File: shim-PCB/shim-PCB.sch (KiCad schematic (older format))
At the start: 24 parts, among them J1 ROMI-Encoder, J10 LineSensor, J11 LineSensor, J12 SPI, J13 Ultrasonic., J14 THING, J15 THING, J16 Conn_01x02_Female, J2 ROMI-Encoder, J3 Conn_01x19_Female, J4 ServoAnalog, J5 Conn_01x19_Female, J6 Conn_01x19_Female, J7 ROMI, J8 ROMI, J9 Conn_01x19_Female

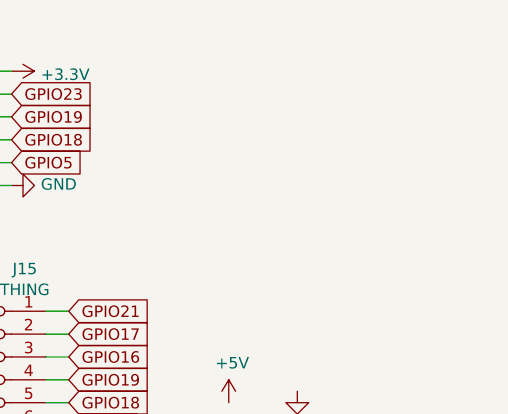
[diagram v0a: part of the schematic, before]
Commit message: Broke out i2c
ISsue #7
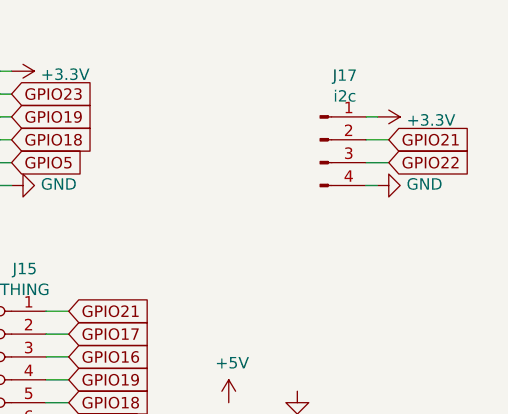
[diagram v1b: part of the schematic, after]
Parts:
- added J17: i2c, Connector_PinSocket_2.54mm:PinSocket_1x04_P2.54mm_Vertical, symbol Connector:Conn_01x04_Male
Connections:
- net +3V3: now also J17.1 (Pin_1)
- net GND: now also J17.4 (Pin_4)
- net GPIO21: now also J17.2 (Pin_2)
- net GPIO22: now also J17.3 (Pin_3)
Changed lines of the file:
@@
 Text Notes 1000 6550 1    50   ~ 0
 Right
+$Comp
+L Connector:Conn_01x04_Male J17
+U 1 1 5F351CBA
+P 7700 1200
+F 0 "J17" H 7808 1481 50  0000 C CNN
+F 1 "i2c" H 7808 1390 50  0000 C CNN
+F 2 "Connector_PinSocket_2.54mm:PinSocket_1x04_P2.54mm_Vertical" H 7700 1200 50  0001 C CNN
+F 3 "~" H 7700 1200 50  0001 C CNN
+	1    7700 1200
+	1    0    0    -1
+$EndComp
+$Comp
+L power:+3.3V #PWR0137
+U 1 1 5F351CC0
+P 7950 1100
+F 0 "#PWR0137" H 7950 950 50  0001 C CNN
+F 1 "+3.3V" V 7965 1228 50  0000 L CNN
+F 2 "" H 7950 1100 50  0001 C CNN
+F 3 "" H 7950 1100 50  0001 C CNN
+	1    7950 1100
+	0    1    1    0
+$EndComp
+$Comp
+L power:GND #PWR0138
+U 1 1 5F351CC6
+P 7950 1400
+F 0 "#PWR0138" H 7950 1150 50  0001 C CNN
+F 1 "GND" V 7955 1272 50  0000 R CNN
+F 2 "" H 7950 1400 50  0001 C CNN
+F 3 "" H 7950 1400 50  0001 C CNN
+	1    7950 1400
+	0    -1   -1   0
+$EndComp
+Wire Wire Line
+	7950 1100 7900 1100
+Wire Wire Line
+	7950 1400 7900 1400
+Text GLabel 8000 1200 2    50   Input ~ 0
+GPIO21
+Text GLabel 8000 1300 2    50   Input ~ 0
+GPIO22
+Wire Wire Line
+	8000 1200 7900 1200
+Wire Wire Line
+	8000 1300 7900 1300
 $EndSCHEMATC

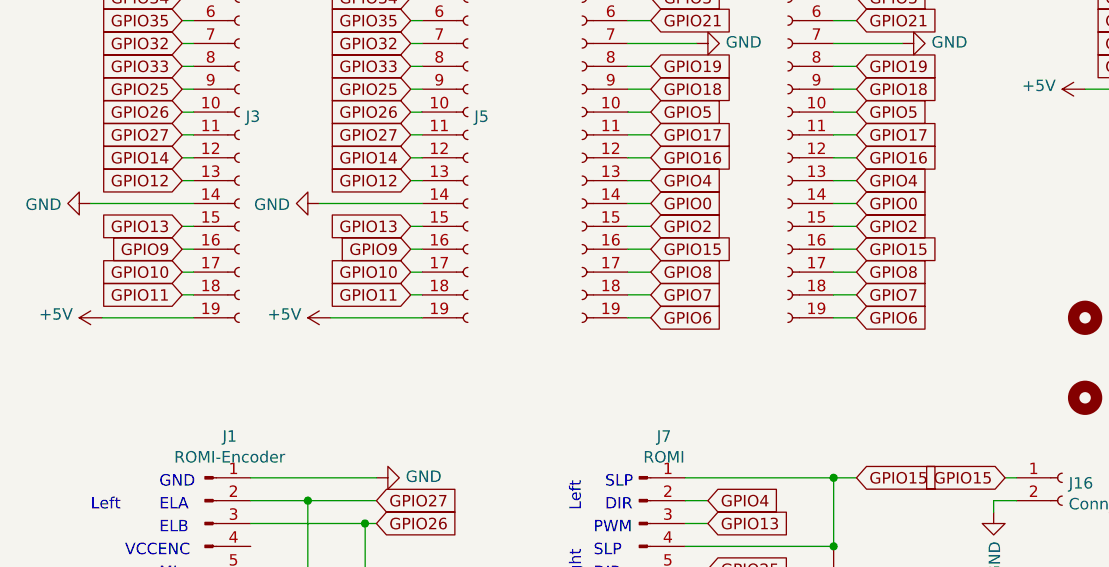
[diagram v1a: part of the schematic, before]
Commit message: Switched to 4 layer. Disconnected flash pins.
Resolved #15
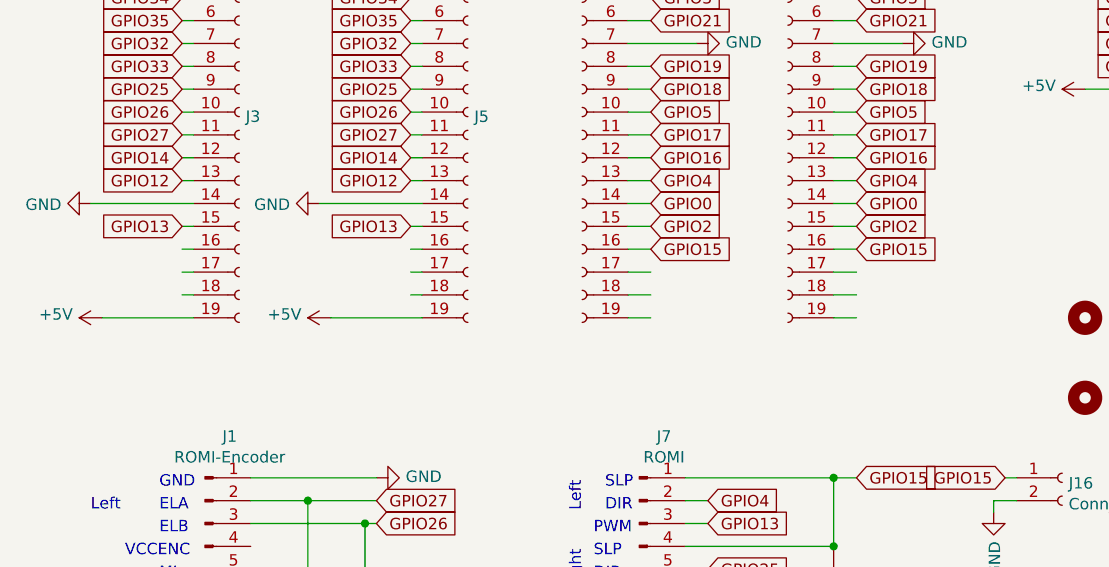
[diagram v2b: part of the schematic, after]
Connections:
- net labels removed: GPIO10, GPIO11, GPIO6, GPIO7, GPIO8, GPIO9
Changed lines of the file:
@@
 Text GLabel 2250 3450 0    50   Input ~ 0
 GPIO13
-Text GLabel 2250 3550 0    50   Input ~ 0
-GPIO9
-Text GLabel 2250 3650 0    50   Input ~ 0
-GPIO10
-Text GLabel 2250 3750 0    50   Input ~ 0
-GPIO11
 $Comp
 L power:+5V #PWR0108
@@
 Text GLabel 3300 3550 2    50   Input ~ 0
 GPIO15
-Text GLabel 3300 3650 2    50   Input ~ 0
-GPIO8
-Text GLabel 3300 3750 2    50   Input ~ 0
-GPIO7
-Text GLabel 3300 3850 2    50   Input ~ 0
-GPIO6
 $Comp
 L power:GND #PWR0129
@@
 Text GLabel 1250 3450 0    50   Input ~ 0
 GPIO13
-Text GLabel 1250 3550 0    50   Input ~ 0
-GPIO9
-Text GLabel 1250 3650 0    50   Input ~ 0
-GPIO10
-Text GLabel 1250 3750 0    50   Input ~ 0
-GPIO11
 $Comp
 L power:+5V #PWR0132
@@
 Text GLabel 4200 3550 2    50   Input ~ 0
 GPIO15
-Text GLabel 4200 3650 2    50   Input ~ 0
-GPIO8
-Text GLabel 4200 3750 2    50   Input ~ 0
-GPIO7
-Text GLabel 4200 3850 2    50   Input ~ 0
-GPIO6
 $Comp
 L power:GND #PWR0134

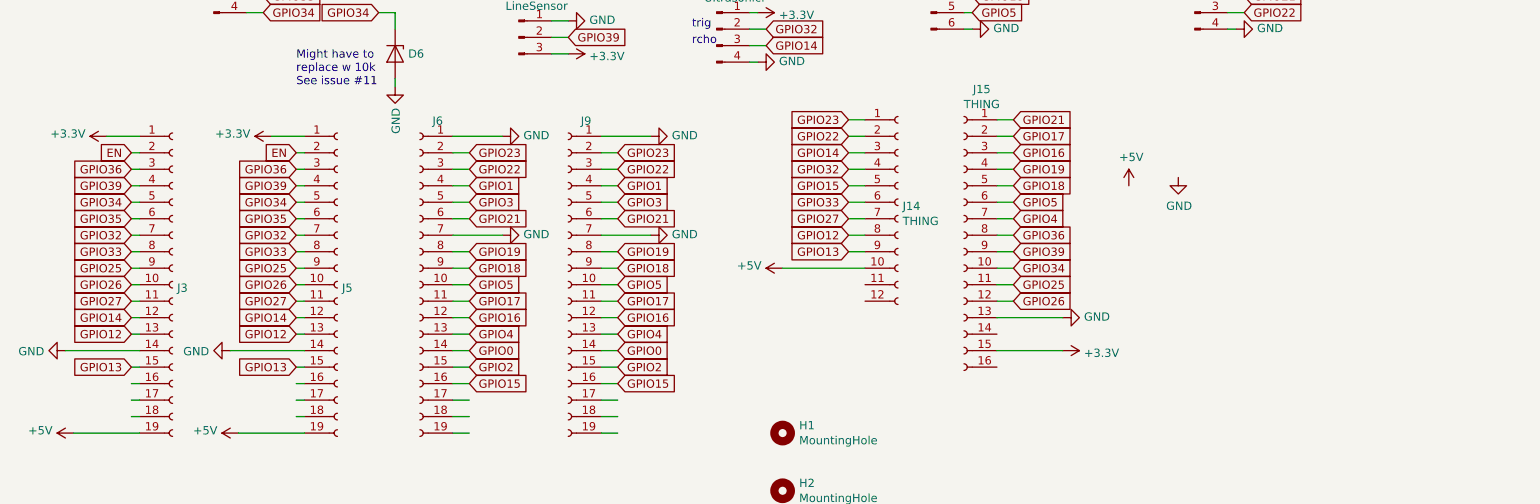
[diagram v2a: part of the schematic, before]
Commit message: Fixed silkscreen
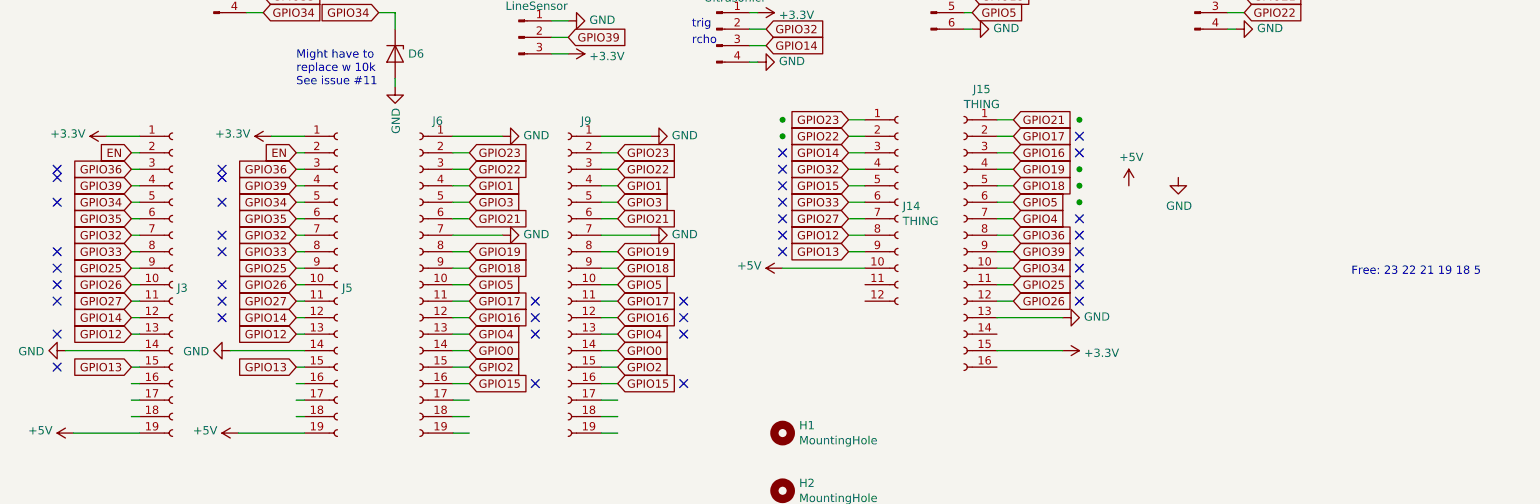
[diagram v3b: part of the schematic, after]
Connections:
- no-connect marks 0 -> 40
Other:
- note added: "Free: 23 22 21 19 18 5"
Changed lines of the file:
@@
 Wire Wire Line
 	8000 1300 7900 1300
+NoConn ~ 1800 2750
+NoConn ~ 1800 2450
+NoConn ~ 800  2450
+NoConn ~ 800  2750
+NoConn ~ 5200 2450
+NoConn ~ 7000 2850
+NoConn ~ 800  2250
+NoConn ~ 800  2300
+NoConn ~ 1800 2250
+NoConn ~ 1800 2300
+NoConn ~ 7000 2650
+NoConn ~ 7000 2750
+NoConn ~ 5200 2150
+NoConn ~ 5200 2250
+NoConn ~ 1800 2650
+NoConn ~ 1800 3150
+NoConn ~ 800  3050
+NoConn ~ 800  2950
+NoConn ~ 3700 3050
+NoConn ~ 3700 3150
+NoConn ~ 4600 3050
+NoConn ~ 4600 3150
+NoConn ~ 7000 2050
+NoConn ~ 7000 2150
+NoConn ~ 1800 3050
+NoConn ~ 1800 2950
+NoConn ~ 5200 2550
+NoConn ~ 7000 3050
+NoConn ~ 7000 2550
+NoConn ~ 5200 2750
+NoConn ~ 4600 3250
+NoConn ~ 800  3450
+NoConn ~ 3700 3250
+NoConn ~ 7000 2950
+NoConn ~ 5200 2650
+NoConn ~ 800  2850
+NoConn ~ 800  3250
+NoConn ~ 3700 3550
+NoConn ~ 4600 3550
+NoConn ~ 5200 2350
+Text Notes 8650 2900 0    50   ~ 0
+Free: 23 22 21 19 18 5
+Connection ~ 5200 1950
+Connection ~ 5200 2050
+Connection ~ 7000 1950
+Connection ~ 7000 2250
+Connection ~ 7000 2350
+Connection ~ 7000 2450
 $EndSCHEMATC

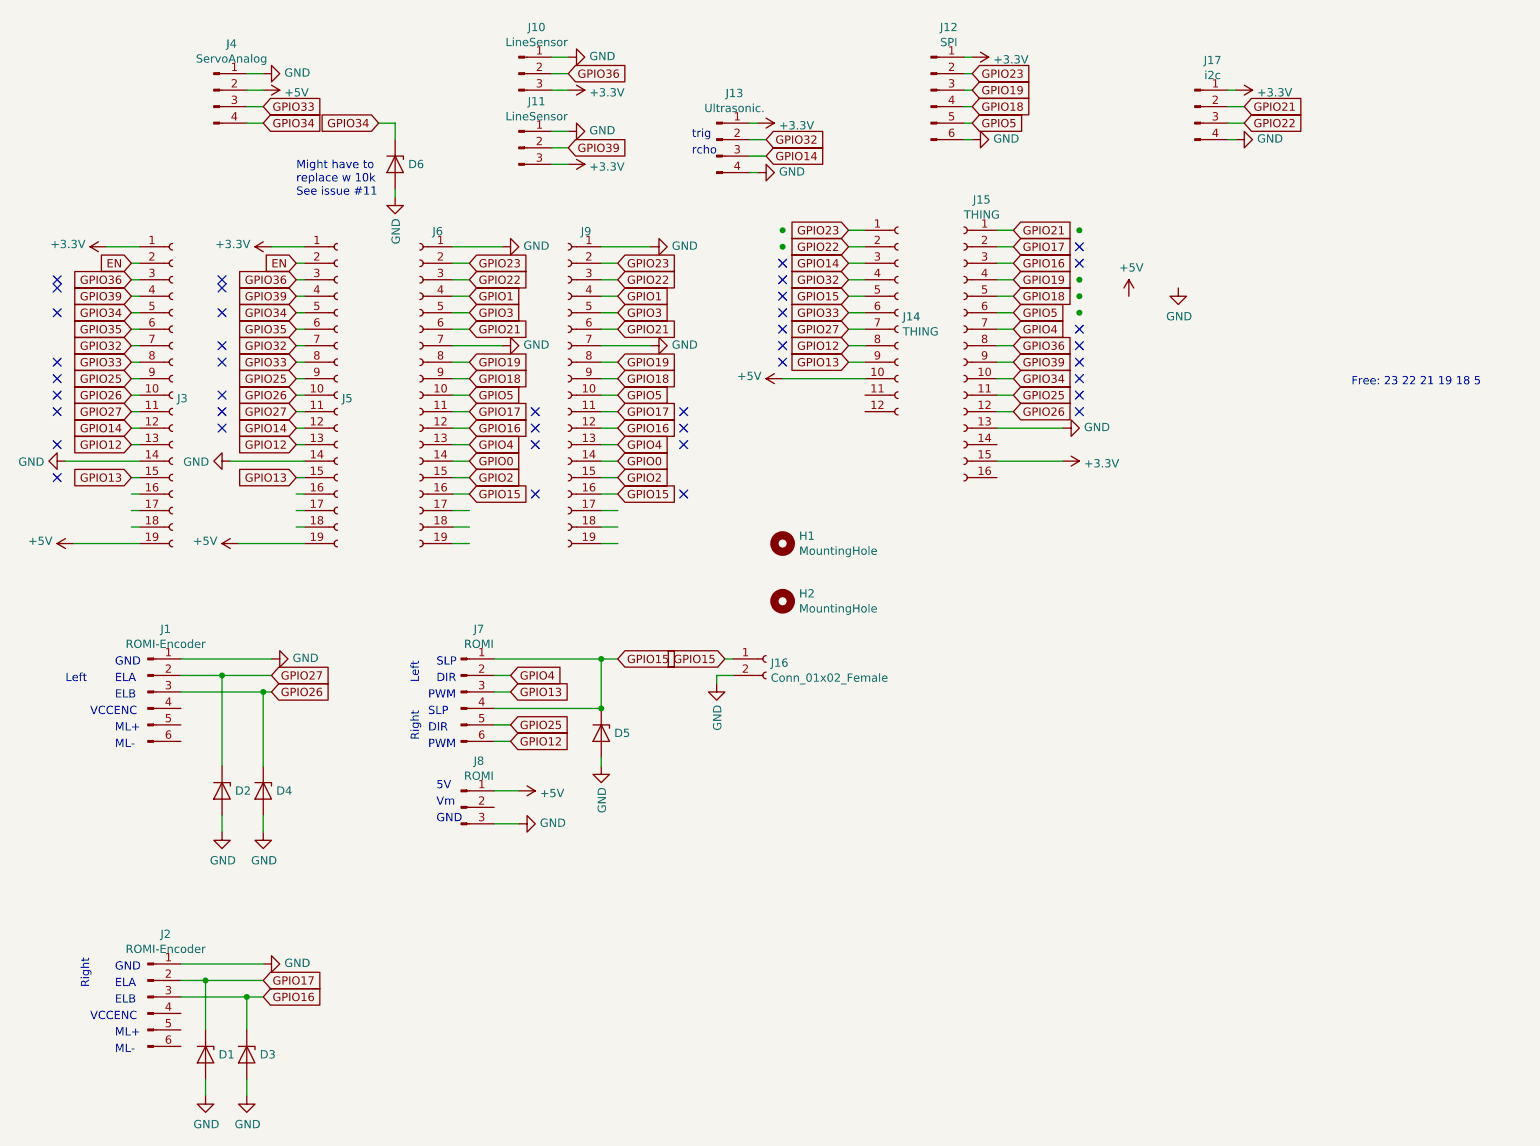
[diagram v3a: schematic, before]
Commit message: new board rev
Added jumper to switch between pins 21 and 23 to resolve conflict with samd21 i2c resolving issue #26

Swapped encoder and ultrasonic pins to resolve conflict with samd21 resolving issue #25
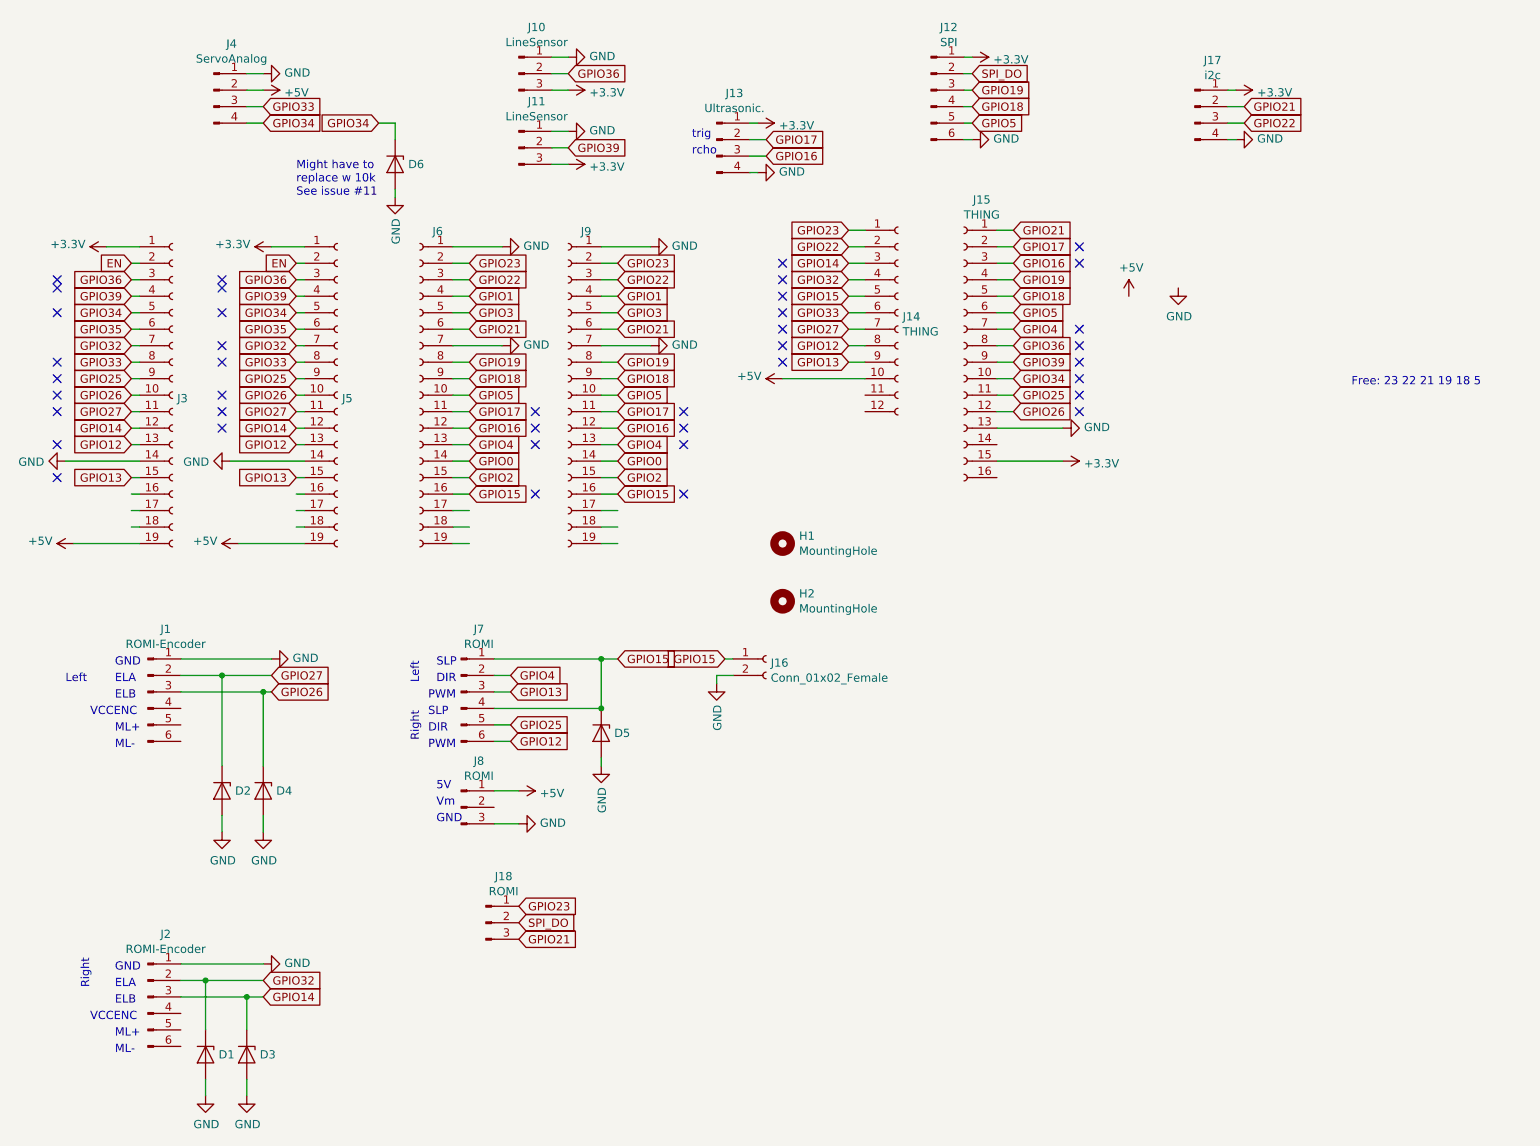
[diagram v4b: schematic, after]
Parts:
- added J18: ROMI, Connector_PinSocket_2.54mm:PinSocket_1x03_P2.54mm_Vertical, symbol Connector:Conn_01x03_Male
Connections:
- net labels added: SPI_DO
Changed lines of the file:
@@
 Text GLabel 2100 4750 2    50   Input ~ 0
 GPIO26
-Text GLabel 2050 6500 2    50   Input ~ 0
+Text GLabel 5100 1400 2    50   Input ~ 0
 GPIO17
-Text GLabel 2050 6600 2    50   Input ~ 0
+Text GLabel 5100 1500 2    50   Input ~ 0
 GPIO16
 $Comp
@@
 Wire Wire Line
 	5050 1600 5000 1600
-Text GLabel 5100 1400 2    50   Input ~ 0
+Text GLabel 2050 6500 2    50   Input ~ 0
 GPIO32
-Text GLabel 5100 1500 2    50   Input ~ 0
+Text GLabel 2050 6600 2    50   Input ~ 0
 GPIO14
 Wire Wire Line
@@
 Wire Wire Line
 	4100 5150 4100 5200
-Text GLabel 6350 1000 2    50   Input ~ 0
-GPIO23
 Text GLabel 6350 1100 2    50   Input ~ 0
 GPIO19
@@
 Text Notes 8650 2900 0    50   ~ 0
 Free: 23 22 21 19 18 5
-Connection ~ 5200 1950
-Connection ~ 5200 2050
-Connection ~ 7000 1950
-Connection ~ 7000 2250
-Connection ~ 7000 2350
-Connection ~ 7000 2450
+$Comp
+L Connector:Conn_01x03_Male J18
+U 1 1 5F126D8C
+P 3400 6150
+F 0 "J18" H 3508 6431 50  0000 C CNN
+F 1 "ROMI" H 3508 6340 50  0000 C CNN
+F 2 "Connector_PinSocket_2.54mm:PinSocket_1x03_P2.54mm_Vertical" H 3400 6150 50  0001 C CNN
+F 3 "~" H 3400 6150 50  0001 C CNN
+	1    3400 6150
+	1    0    0    -1
+$EndComp
+Text GLabel 3600 6050 2    50   Input ~ 0
+GPIO23
+Text GLabel 3600 6250 2    50   Input ~ 0
+GPIO21
+Text GLabel 6350 1000 2    50   Input ~ 0
+SPI_DO
+Text GLabel 3600 6150 2    50   Input ~ 0
+SPI_DO
 $EndSCHEMATC

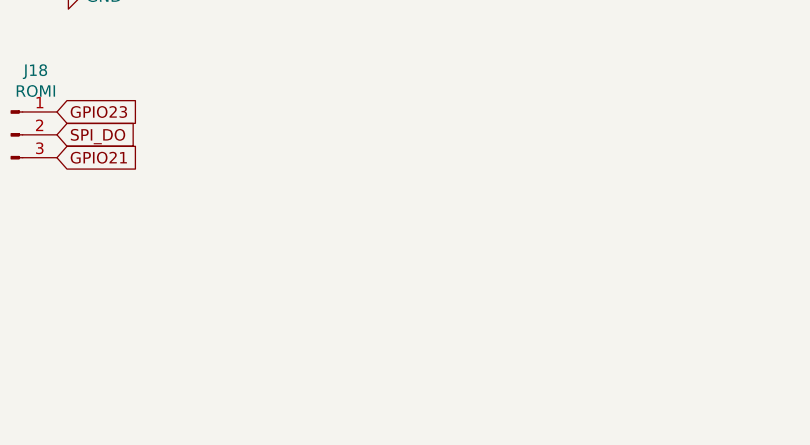
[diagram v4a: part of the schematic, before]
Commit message: tied artwork to component
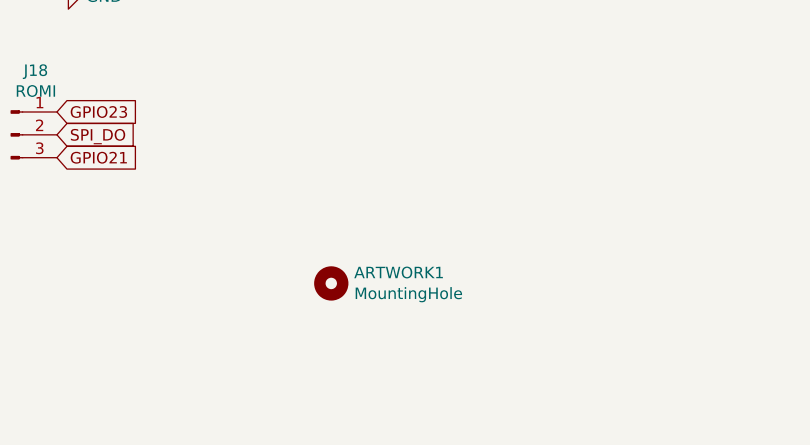
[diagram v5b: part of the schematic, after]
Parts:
- added ARTWORK1: MountingHole, shim-PCB:silkscreen, symbol Mechanical:MountingHole
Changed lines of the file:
@@
 Text GLabel 3600 6150 2    50   Input ~ 0
 SPI_DO
+$Comp
+L Mechanical:MountingHole ARTWORK1
+U 1 1 5F13092A
+P 4800 6800
+F 0 "ARTWORK1" H 4900 6846 50  0000 L CNN
+F 1 "MountingHole" H 4900 6755 50  0000 L CNN
+F 2 "shim-PCB:silkscreen" H 4800 6800 50  0001 C CNN
+F 3 "~" H 4800 6800 50  0001 C CNN
+	1    4800 6800
+	1    0    0    -1
+$EndComp
 $EndSCHEMATC
